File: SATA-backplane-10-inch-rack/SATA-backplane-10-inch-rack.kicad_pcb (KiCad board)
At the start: 2 copper layers, 236.2 x 48.3 mm, 32 parts, among them J1001 67800-5001, J1002 1735284-2, J101 Barrel_Jack_Switch_Pin3Ring, J1101 67800-5001, J1102 1735284-2, J1201 67800-5001, J1202 1735284-2, J1301 67800-5001, J1302 1735284-2, J201 67800-5001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

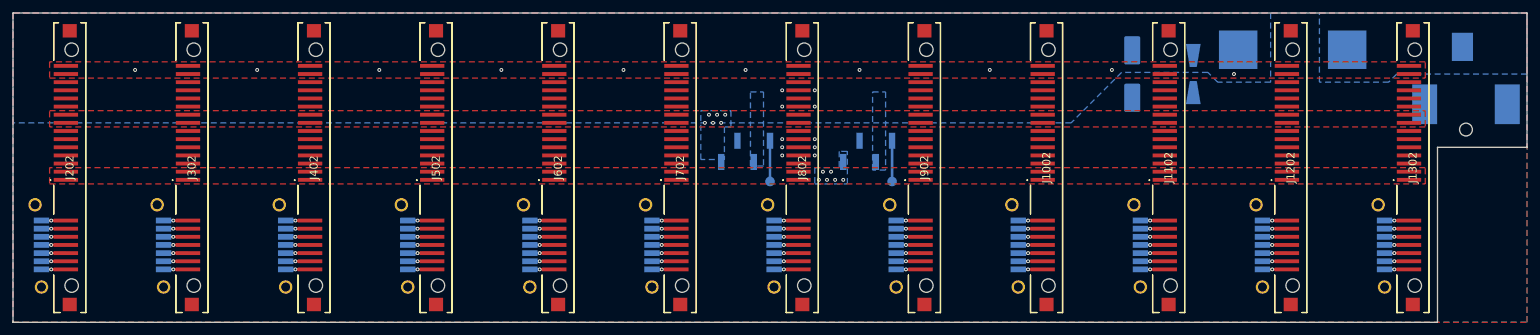
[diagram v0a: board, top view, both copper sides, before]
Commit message: More realistic layout
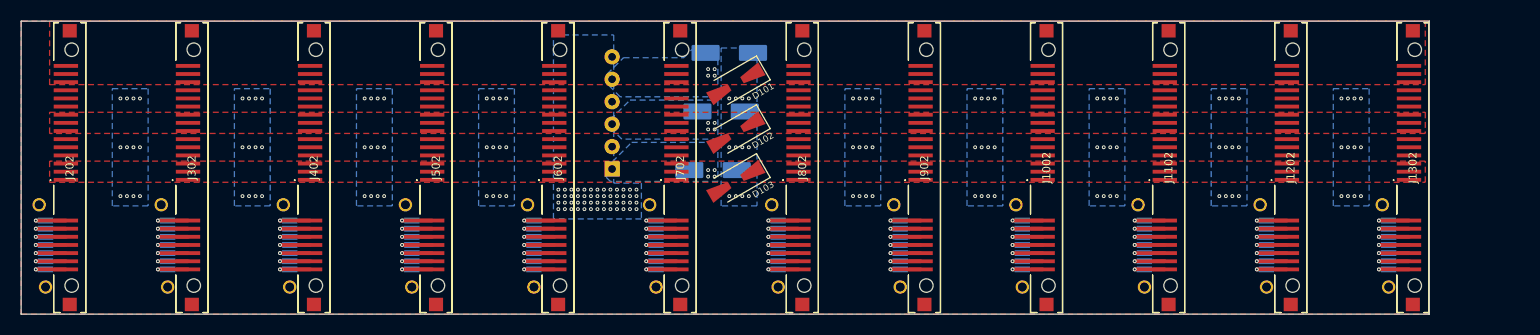
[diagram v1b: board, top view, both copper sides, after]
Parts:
- removed F101: Fuseholder, Libraries:Fuseholder_Cylinder-5x20mm_Wuerth_696103101002-SMD_Horizontal_Open
- removed TP101, TP102: TestPoint, TestPoint:TestPoint_Pad_D1.5mm
- removed U101: HW-613 5V0, Libraries:HW-613
- removed U102: HW-613 3V3, Libraries:HW-613
- added C102: 100uF 25V, Capacitor_SMD:CP_Elec_8x10.5, B.Cu at (142.2, 45.2)
- added C103: 100uF 25V, Capacitor_SMD:CP_Elec_8x10.5, B.Cu at (141.0, 54.4)
- added D102: SMAJ5.0A, Diode_SMD:D_SMA-SMB_Universal_Handsoldering, F.Cu at (144.5, 48.5)
- added D103: SMF3.3, Diode_SMD:D_SMA-SMB_Universal_Handsoldering, F.Cu at (144.5, 56.1)
- D101: moved to F.Cu
- J101: value Barrel_Jack_Switch_Pin3Ring -> Conn_01x06; footprint Libraries:PJ036AHSMTTR -> TerminalBlock_Phoenix:TerminalBlock_Phoenix_PT-1,5-6-3.5-H_1x06_P3.50mm_Horizontal
- moved J101 133.8 mm to (125.2, 54.2), turned to 90 degrees
- moved D101 71.4 mm to (144.5, 40.9), turned to -150 degrees
- moved C101 63.0 mm to (143.5, 36.1), turned to 0 degrees
- moved J1201 0.64 mm to (223.3, 74.5)
- moved J701 0.64 mm to (128.1, 74.5)
- moved J901 0.64 mm to (166.2, 74.5)
- moved J301 0.64 mm to (51.9, 74.5)
- moved J401 0.64 mm to (70.9, 74.5)
- moved J501 0.64 mm to (90.0, 74.5)
- moved J601 0.64 mm to (109.0, 74.5)
- moved J201 0.63 mm to (32.8, 74.5)
- moved J1001 0.63 mm to (185.2, 74.5)
- moved J1101 0.63 mm to (204.3, 74.5)
- moved J1301 0.63 mm to (242.4, 74.5)
- moved J801 0.63 mm to (147.1, 74.5)
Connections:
- net /Port_1/ACT renamed /Port_1/ACT/STA
- net /Port_10/ACT renamed /Port_10/ACT/STA
- net /Port_11/ACT renamed /Port_11/ACT/STA
- net /Port_12/ACT renamed /Port_12/ACT/STA
- net /Port_2/ACT renamed /Port_2/ACT/STA
- net /Port_3/ACT renamed /Port_3/ACT/STA
- net /Port_4/ACT renamed /Port_4/ACT/STA
- net /Port_5/ACT renamed /Port_5/ACT/STA
- net /Port_6/ACT renamed /Port_6/ACT/STA
- net /Port_7/ACT renamed /Port_7/ACT/STA
- net /Port_8/ACT renamed /Port_8/ACT/STA
- net /Port_9/ACT renamed /Port_9/ACT/STA
- J1002 pad MP2: GND -> +12V
- J1002 pad P13: /Port_9/12V0_P -> +12V
- J1002 pad P3: /Port_9/3V3_PWDIS -> +3.3V
- J1002 pad P7: /Port_9/5V0_P -> +5V
- J101 pad 1: Net-(F101-Pad2) -> +3.3V
- J101 pad 2: unconnected-(J101-Pad2) -> GND
- J101 pad 3: GND -> +5V
- J1102 pad MP2: GND -> +12V
- J1102 pad P13: /Port_10/12V0_P -> +12V
- J1102 pad P3: /Port_10/3V3_PWDIS -> +3.3V
- J1102 pad P7: /Port_10/5V0_P -> +5V
- J1202 pad MP2: GND -> +12V
- J1202 pad P13: /Port_11/12V0_P -> +12V
- J1202 pad P3: /Port_11/3V3_PWDIS -> +3.3V
- J1202 pad P7: /Port_11/5V0_P -> +5V
- J1302 pad MP2: GND -> +12V
- J1302 pad P13: /Port_12/12V0_P -> +12V
- J1302 pad P3: /Port_12/3V3_PWDIS -> +3.3V
- J1302 pad P7: /Port_12/5V0_P -> +5V
- J202 pad MP2: GND -> +12V
- J202 pad P13: /Port_1/12V0_P -> +12V
- J202 pad P3: /Port_1/3V3_PWDIS -> +3.3V
- J202 pad P7: /Port_1/5V0_P -> +5V
- J302 pad MP2: GND -> +12V
- J302 pad P13: /Port_2/12V0_P -> +12V
- J302 pad P3: /Port_2/3V3_PWDIS -> +3.3V
- J302 pad P7: /Port_2/5V0_P -> +5V
- J402 pad MP2: GND -> +12V
- J402 pad P13: /Port_3/12V0_P -> +12V
- J402 pad P3: /Port_3/3V3_PWDIS -> +3.3V
- J402 pad P7: /Port_3/5V0_P -> +5V
- J502 pad MP2: GND -> +12V
- J502 pad P13: /Port_4/12V0_P -> +12V
- J502 pad P3: /Port_4/3V3_PWDIS -> +3.3V
- J502 pad P7: /Port_4/5V0_P -> +5V
- J602 pad MP2: GND -> +12V
- J602 pad P13: /Port_5/12V0_P -> +12V
- J602 pad P3: /Port_5/3V3_PWDIS -> +3.3V
- J602 pad P7: /Port_5/5V0_P -> +5V
- J702 pad MP2: GND -> +12V
- J702 pad P13: /Port_6/12V0_P -> +12V
- J702 pad P3: /Port_6/3V3_PWDIS -> +3.3V
- J702 pad P7: /Port_6/5V0_P -> +5V
- J802 pad MP2: GND -> +12V
- J802 pad P13: /Port_7/12V0_P -> +12V
- J802 pad P3: /Port_7/3V3_PWDIS -> +3.3V
- J802 pad P7: /Port_7/5V0_P -> +5V
- J902 pad MP2: GND -> +12V
- J902 pad P13: /Port_8/12V0_P -> +12V
- J902 pad P3: /Port_8/3V3_PWDIS -> +3.3V
- J902 pad P7: /Port_8/5V0_P -> +5V
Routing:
- net GND: track 137.2 -> 224.0 mm, vias 46 -> 208
- net /EN: track 12.7 -> 0.00 mm
- net /Port_9/B-: track 3.81 -> 6.22 mm
- net /Port_9/B+: track 3.81 -> 6.22 mm
- net /Port_9/A-: track 3.81 -> 6.22 mm
- net /Port_9/A+: track 3.81 -> 6.22 mm
- net /Port_7/B-: track 3.81 -> 6.22 mm
- net /Port_7/B+: track 3.81 -> 6.22 mm
- net /Port_7/A-: track 3.81 -> 6.22 mm
- net /Port_7/A+: track 3.81 -> 6.22 mm
- net /Port_12/B-: track 3.81 -> 6.22 mm
- net /Port_12/B+: track 3.81 -> 6.22 mm
- net /Port_12/A-: track 3.81 -> 6.22 mm
- net /Port_12/A+: track 3.81 -> 6.22 mm
- net /Port_10/B-: track 3.81 -> 6.22 mm
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- removed copper zone on B.Cu, net Net-(F101-Pad2)
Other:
- board size 236.2 x 48.3 mm -> 219.7 x 45.7 mm
- board text added: "GND 12V GND 5V GND 3.3V"

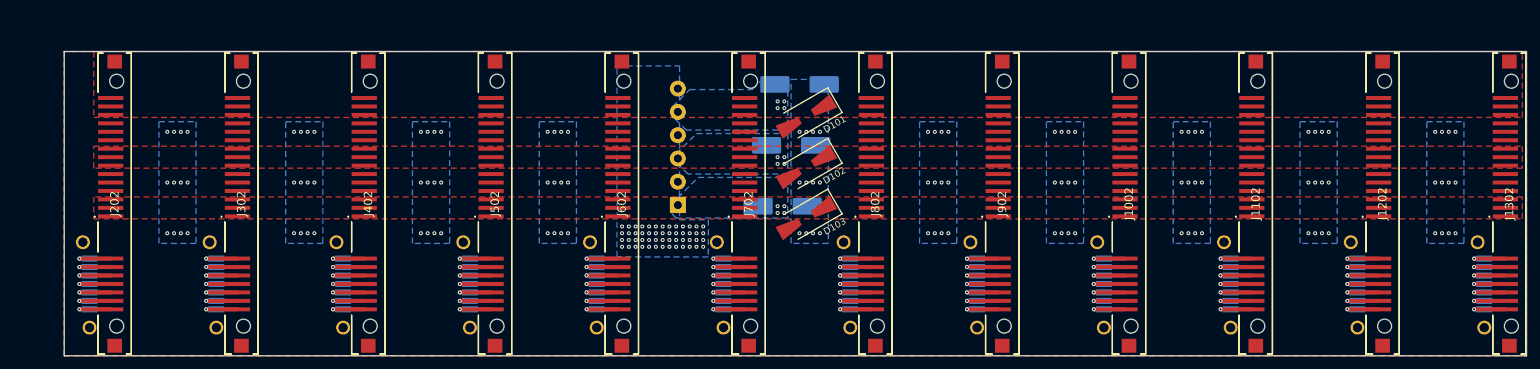
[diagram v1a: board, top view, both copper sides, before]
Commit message: STA/ACT implemented in layout
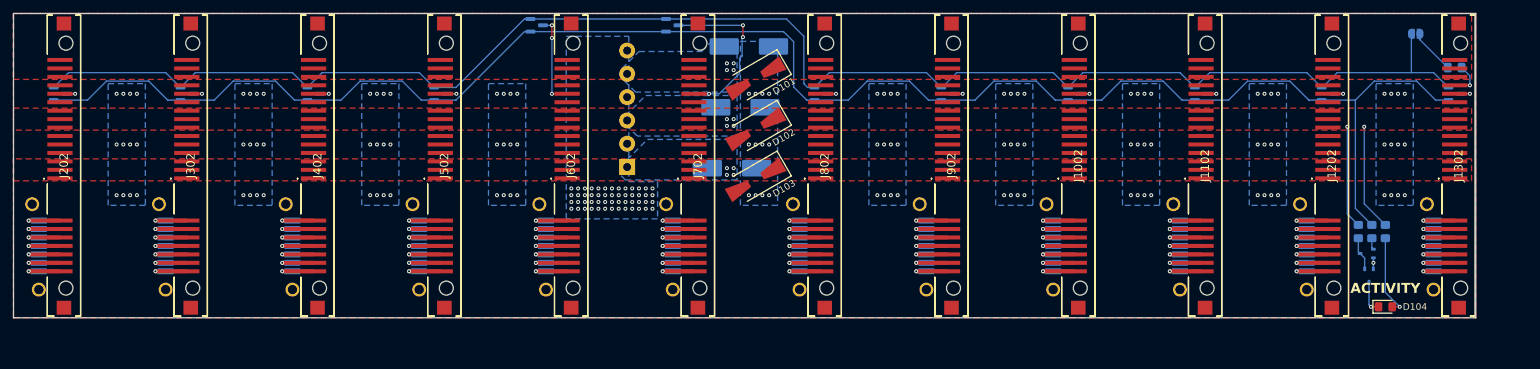
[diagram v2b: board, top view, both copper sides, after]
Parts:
- added C104: 10uF 6.3V, Capacitor_SMD:C_0805_2012Metric_Pad1.18x1.45mm_HandSolder, B.Cu at (241.9, 33.5)
- added D1001: BAT54S, Package_TO_SOT_SMD:SOT-23, B.Cu at (184.8, 37.5)
- added D104: Yellow, LED_SMD:LED_0805_2012Metric_Pad1.15x1.40mm_HandSolder, F.Cu at (231.5, 69.5)
- added D1101: BAT54S, Package_TO_SOT_SMD:SOT-23, B.Cu at (203.8, 37.5)
- added D1201: BAT54S, Package_TO_SOT_SMD:SOT-23, B.Cu at (222.9, 37.5)
- added D1301: BAT54S, Package_TO_SOT_SMD:SOT-23, B.Cu at (241.9, 37.5)
- added D201: BAT54S, Package_TO_SOT_SMD:SOT-23, B.Cu at (32.4, 37.5)
- added D301: BAT54S, Package_TO_SOT_SMD:SOT-23, B.Cu at (51.4, 37.5)
- added D401: BAT54S, Package_TO_SOT_SMD:SOT-23, B.Cu at (70.5, 37.5)
- added D501: BAT54S, Package_TO_SOT_SMD:SOT-23, B.Cu at (89.5, 37.5)
- added D601: BAT54S, Package_TO_SOT_SMD:SOT-23, B.Cu at (104.0, 27.2)
- added D701: BAT54S, Package_TO_SOT_SMD:SOT-23, B.Cu at (124.4, 27.2)
- added D801: BAT54S, Package_TO_SOT_SMD:SOT-23, B.Cu at (146.7, 37.5)
- added D901: BAT54S, Package_TO_SOT_SMD:SOT-23, B.Cu at (165.7, 37.5)
- added JP101: SolderJumper, Jumper:SolderJumper-2_P1.3mm_Open_RoundedPad1.0x1.5mm, B.Cu at (236.1, 28.4)
- added Q101: DMG1012UW, Package_TO_SOT_SMD:SOT-323_SC-70, B.Cu at (229.1, 64.8)
- added Q102: DMG1012UW, Package_TO_SOT_SMD:SOT-323_SC-70, B.Cu at (228.7, 61.5)
- added R101: 270R, Resistor_SMD:R_0805_2012Metric_Pad1.20x1.40mm_HandSolder, B.Cu at (231.5, 58.2)
- added R102: 100k, Resistor_SMD:R_0805_2012Metric_Pad1.20x1.40mm_HandSolder, B.Cu at (229.5, 58.2)
- added R103: 1M, Resistor_SMD:R_0805_2012Metric_Pad1.20x1.40mm_HandSolder, B.Cu at (227.5, 58.2)
- moved J701 9.53 mm to (120.5, 68.8)
- moved C102 9.53 mm to (134.6, 39.5)
- moved C103 9.53 mm to (133.3, 48.6)
- moved D102 9.53 mm to (136.9, 42.8)
- moved D103 9.53 mm to (136.9, 50.4)
- moved J1002 9.53 mm to (185.4, 48.3)
- moved J1102 9.53 mm to (204.4, 48.3)
- moved J1302 9.53 mm to (242.5, 48.3)
- moved J302 9.53 mm to (52.0, 48.3)
- moved J402 9.53 mm to (71.1, 48.3)
- moved J602 9.53 mm to (109.2, 48.3)
- moved J802 9.53 mm to (147.3, 48.3)
- moved J902 9.53 mm to (166.3, 48.3)
- moved C101 9.53 mm to (135.9, 30.4)
- moved D101 9.53 mm to (136.9, 35.2)
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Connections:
- J1002 pad P11: /Port_9/ACT/STA -> /Port_9/STA/ACT
- J1102 pad P11: /Port_10/ACT/STA -> /Port_10/STA/ACT
- J1202 pad P11: /Port_11/ACT/STA -> /Port_11/STA/ACT
- J1302 pad P11: /Port_12/ACT/STA -> /Port_12/STA/ACT
- J202 pad P11: /Port_1/ACT/STA -> /Port_1/STA/ACT
- J302 pad P11: /Port_2/ACT/STA -> /Port_2/STA/ACT
- J402 pad P11: /Port_3/ACT/STA -> /Port_3/STA/ACT
- J502 pad P11: /Port_4/ACT/STA -> /Port_4/STA/ACT
- J602 pad P11: /Port_5/ACT/STA -> /Port_5/STA/ACT
- J702 pad P11: /Port_6/ACT/STA -> /Port_6/STA/ACT
- J802 pad P11: /Port_7/ACT/STA -> /Port_7/STA/ACT
- J902 pad P11: /Port_8/ACT/STA -> /Port_8/STA/ACT
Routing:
- net ACT: track 0.00 -> 260.8 mm
- net STA_N: track 0.00 -> 242.8 mm
- net +5V: track 0.00 -> 31.5 mm, vias 4 -> 6
- net /Port_6/STA/ACT: track 0.00 -> 25.3 mm, vias 0 -> 3
- net /Port_5/STA/ACT: track 0.00 -> 13.9 mm, vias 0 -> 3
- net Net-(D104-A): track 0.00 -> 12.3 mm, vias 0 -> 1
- net GND: track 224.0 -> 231.2 mm, vias 208 -> 210
- net Net-(JP101-A): track 0.00 -> 6.81 mm
- net Net-(Q101-G): track 0.00 -> 5.00 mm
- net Net-(D104-K): track 0.00 -> 4.96 mm, vias 0 -> 1
- net /Port_4/STA/ACT: track 0.00 -> 3.89 mm, vias 0 -> 1
- net /Port_9/STA/ACT: track 0.00 -> 3.63 mm, vias 0 -> 1
- net /Port_7/STA/ACT: track 0.00 -> 3.63 mm, vias 0 -> 1
- net /Port_3/STA/ACT: track 0.00 -> 3.63 mm, vias 0 -> 1
- net /Port_12/STA/ACT: track 0.00 -> 3.63 mm, vias 0 -> 1
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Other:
- board text added: "ACTIVITY"
- board text added: "GND/black +12V/yellow GND/black +5V/red GND/black +3.3V/orange"
- board text added: "SPNIUP | J101 ----------+------ Staggered | Open Forced | Closed"
- board text removed: "GND 12V GND 5V GND 3.3V"

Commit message: add capacitor discharge
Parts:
- added R104: 1M, Resistor_SMD:R_0805_2012Metric_Pad1.20x1.40mm_HandSolder, B.Cu at (239.9, 28.6)
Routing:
- net GND: track 231.2 -> 238.4 mm
- net STA_N: track 242.8 -> 237.3 mm
- net ACT: track 260.8 -> 255.7 mm
- net Net-(JP101-A): track 6.81 -> 8.01 mm

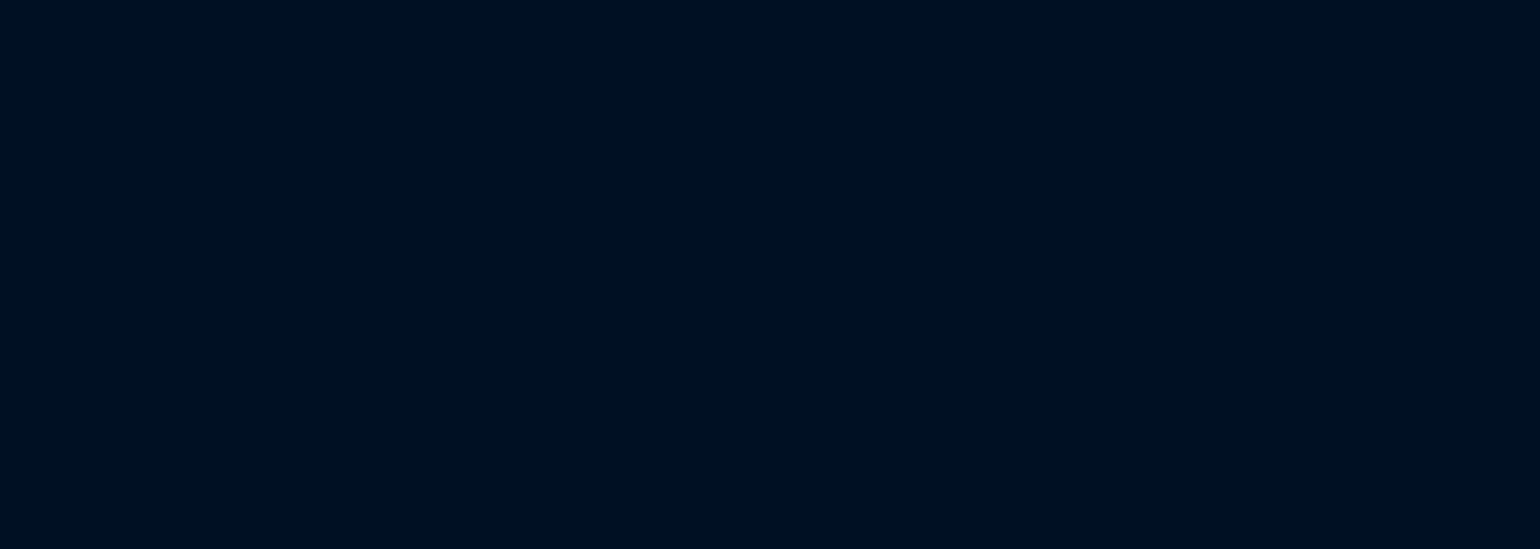
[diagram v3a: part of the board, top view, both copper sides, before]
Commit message: Add 6 x 3½" HDD outline and measures
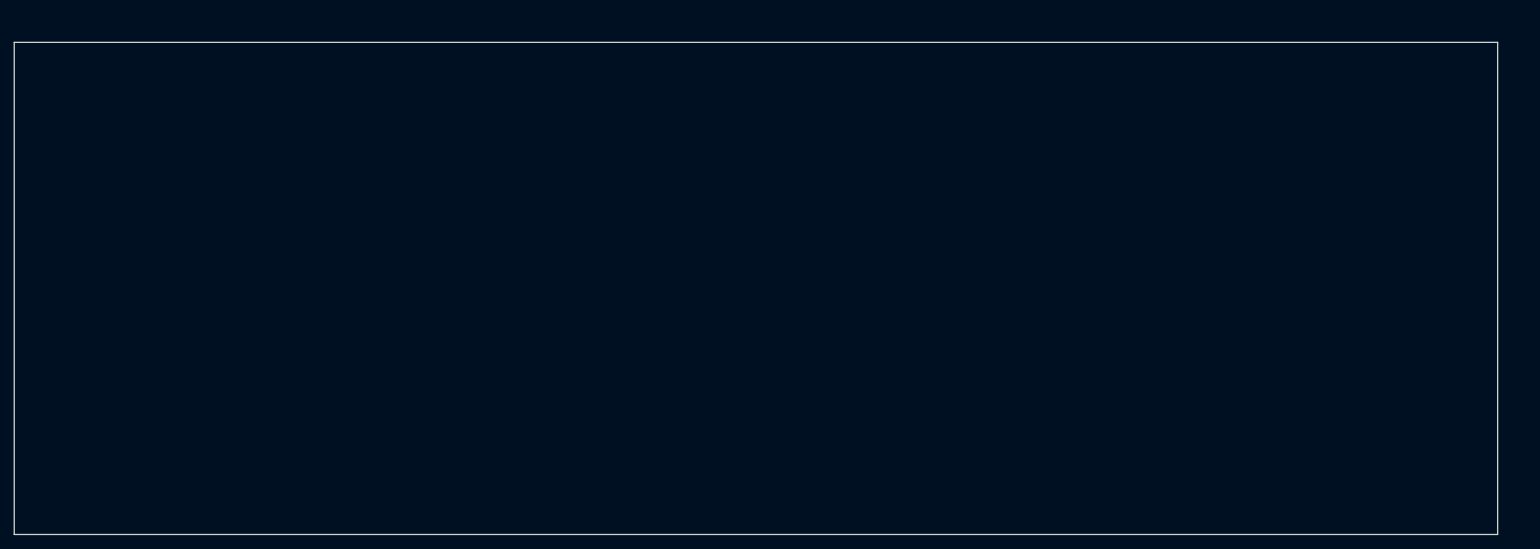
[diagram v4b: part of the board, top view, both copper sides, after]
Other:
- board size 219.7 x 45.7 mm -> 219.7 x 140 mm

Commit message: Adapt to 6 x 3½" version using the multichannel tool
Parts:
- removed D1001, D1101, D1201, D1301, D801, D901: BAT54S, Package_TO_SOT_SMD:SOT-23
- removed J1001, J1101, J1201, J1301, J801, J901: 67800-5001, Libraries:67800-5005_2
- removed J1002, J1102, J1202, J1302, J802, J902: 1735284-2, Libraries:17352842
- C101, C102, C103, C104, D201, D301, D401, D501, D601, D701, J101, J201, J301, J401, J501, J601, J701, JP101, Q101, Q102, R103: moved to F.Cu
- D101, D102, D103, D104, J202, J302, J402, J502, J602, J702: moved to B.Cu
- R101: renamed from R104; moved to F.Cu
- R102: renamed from R101; moved to F.Cu
- R104: renamed from R102; moved to F.Cu
- moved C101 231.7 mm to (339.6, 140.7)
- moved D101 227.2 mm to (340.6, 135.9), turned to 150 degrees
- moved C102 223.5 mm to (338.3, 131.6)
- moved D102 220.9 mm to (340.6, 128.3), turned to 150 degrees
- moved J101 216.8 mm to (321.3, 122.6), turned to -90 degrees
- moved C103 216.7 mm to (337.0, 122.4)
- moved D103 215.5 mm to (340.6, 120.7), turned to 150 degrees
- moved D201 214.9 mm to (223.3, 136.0)
- moved J202 205.9 mm to (223.9, 125.2), turned to -90 degrees
- moved J201 194.3 mm to (216.1, 104.7), turned to -90 degrees
- moved D301 169.5 mm to (189.3, 136.0)
- moved J302 157.9 mm to (189.9, 125.2), turned to -90 degrees
- moved J301 142.5 mm to (182.1, 104.7), turned to -90 degrees
- moved D401 130.0 mm to (155.3, 136.0)
- moved D701 130.0 mm to (53.3, 136.0)
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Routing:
- net ACT: track 255.7 -> 0.00 mm
- net STA_N: track 237.3 -> 0.00 mm
- net GND: track 238.4 -> 120.9 mm, vias 210 -> 155
- net +5V: track 31.5 -> 0.00 mm, vias 6 -> 4
- net /Port_8/B-: track 6.22 -> 0.00 mm, vias 1 -> 0
- net /Port_8/B+: track 6.22 -> 0.00 mm, vias 1 -> 0
- net /Port_8/A-: track 6.22 -> 0.00 mm, vias 1 -> 0
- net /Port_8/A+: track 6.22 -> 0.00 mm, vias 1 -> 0
- net /Port_7/B-: track 6.22 -> 0.00 mm, vias 1 -> 0
- net /Port_7/B+: track 6.22 -> 0.00 mm, vias 1 -> 0
- net /Port_7/A-: track 6.22 -> 0.00 mm, vias 1 -> 0
- net /Port_7/A+: track 6.22 -> 0.00 mm, vias 1 -> 0
- net /Port_12/B-: track 6.22 -> 0.00 mm, vias 1 -> 0
- net /Port_12/B+: track 6.22 -> 0.00 mm, vias 1 -> 0
- net /Port_12/A-: track 6.22 -> 0.00 mm, vias 1 -> 0
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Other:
- board size 219.7 x 140 mm -> 211 x 70 mm
- board text removed: "SPNIUP | J101 ----------+------ Staggered | Open Forced | Closed"

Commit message: Align outline and mounting holes with Jeppe
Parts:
- added H1: MountingHole, MountingHole:MountingHole_3.7mm, F.Cu at (101.1, 163.4)
- added H2: MountingHole, MountingHole:MountingHole_3.7mm, F.Cu at (26.4, 162.3)
- added H3: MountingHole, MountingHole:MountingHole_3.7mm, F.Cu at (169.1, 163.4)
- added H4: MountingHole, MountingHole:MountingHole_3.7mm, F.Cu at (26.4, 106.8)
- added H5: MountingHole, MountingHole:MountingHole_3.7mm, F.Cu at (233.7, 106.8)
- added H6: MountingHole, MountingHole:MountingHole_3.7mm, F.Cu at (233.7, 162.3)
- added R105: 100k, Resistor_SMD:R_0805_2012Metric_Pad1.20x1.40mm_HandSolder, F.Cu at (273.5, 137.1)
- C104: value 10uF 6.3V -> 100uF 6.3V; footprint Capacitor_SMD:C_0805_2012Metric_Pad1.18x1.45mm_HandSolder -> Capacitor_SMD:C_1210_3225Metric_Pad1.33x2.70mm_HandSolder
- moved Q101 91.1 mm to (273.8, 148.3)
- moved R103 91.1 mm to (275.4, 141.7)
- moved R104 91.1 mm to (273.4, 141.7)
- moved D104 91.1 mm to (271.4, 153.0)
- moved Q102 91.1 mm to (274.2, 145.0)
- moved R102 91.1 mm to (271.4, 141.7)
- moved C104 87.3 mm to (199.0, 117.0)
- moved JP101 87.3 mm to (204.8, 111.9)
- moved R101 87.3 mm to (201.0, 112.1)
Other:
- board size 211 x 70 mm -> 210.1 x 69.6 mm

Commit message: Prepare layout
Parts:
- moved C101 209.6 mm to (139.2, 79.2)
- moved J101 209.6 mm to (121.0, 61.1)
- moved C102 209.6 mm to (138.0, 70.1)
- moved C103 209.6 mm to (136.7, 60.9)
- moved D101 209.6 mm to (140.3, 74.4)
- moved D102 209.6 mm to (140.3, 66.8)
- moved D103 209.6 mm to (140.3, 59.2)
- moved Q101 122.9 mm to (174.5, 75.9)
- moved Q102 122.9 mm to (174.9, 72.6)
- moved R104 122.9 mm to (174.1, 69.3)
- moved R105 122.9 mm to (174.2, 64.7)
- moved D104 122.9 mm to (172.1, 80.6)
- moved R102 122.9 mm to (172.1, 69.3)
- moved R103 122.9 mm to (176.1, 69.3)
- moved C104 42.1 mm to (205.2, 75.4)
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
